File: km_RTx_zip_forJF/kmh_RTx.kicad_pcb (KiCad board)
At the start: 2 copper layers, 50 x 40 mm, 54 parts, among them IC2 UA78M33QDCYRG4Q1, J1 Conn_01x06_Pin, T1 ADT16-1T+, T2 ADT16-1T+, U1 AD4PS-1+, U2 BD00D0AWHFP-TR, X1 ASSFLP-R-C02, X2 ASSFLP-R-C02, X3 ASSFLP-R-C02, X4 ASSFLP-R-C02

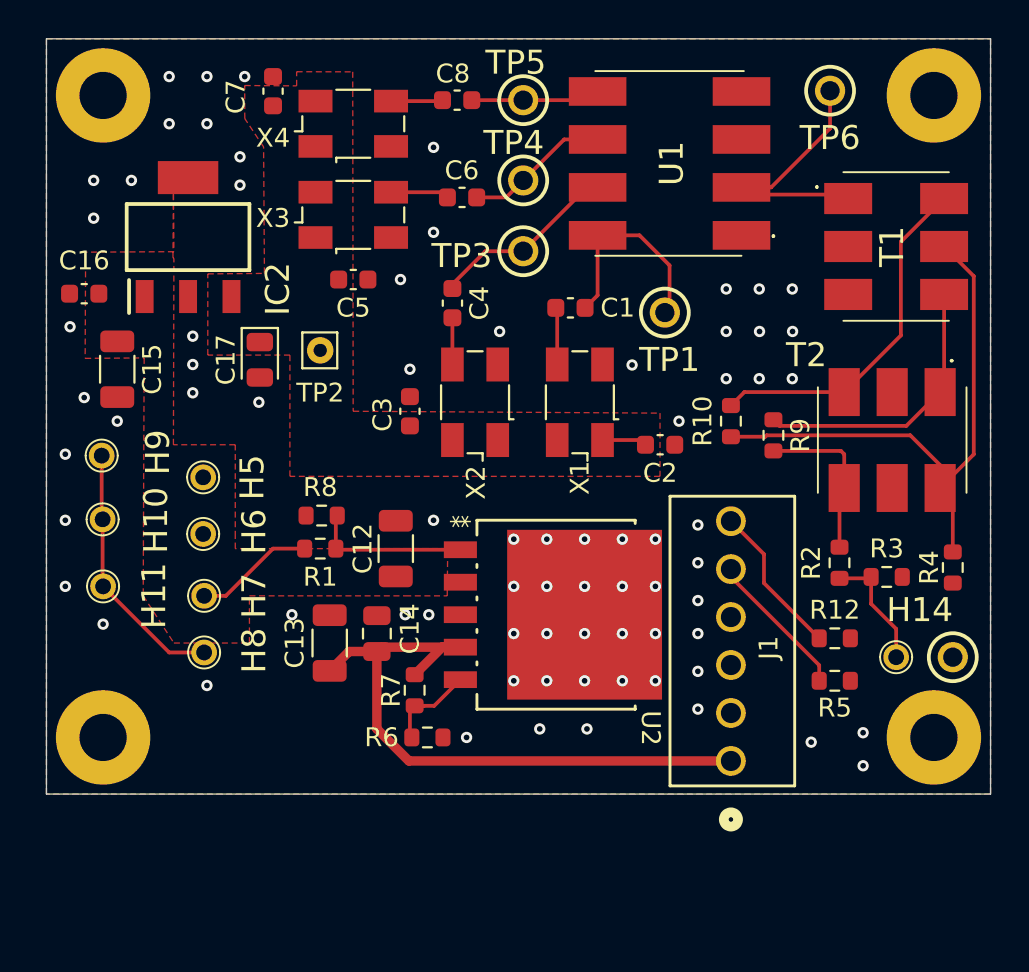
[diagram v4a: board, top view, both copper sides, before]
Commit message: added 2 bit buffers, which replace the previous 8 bit buffers
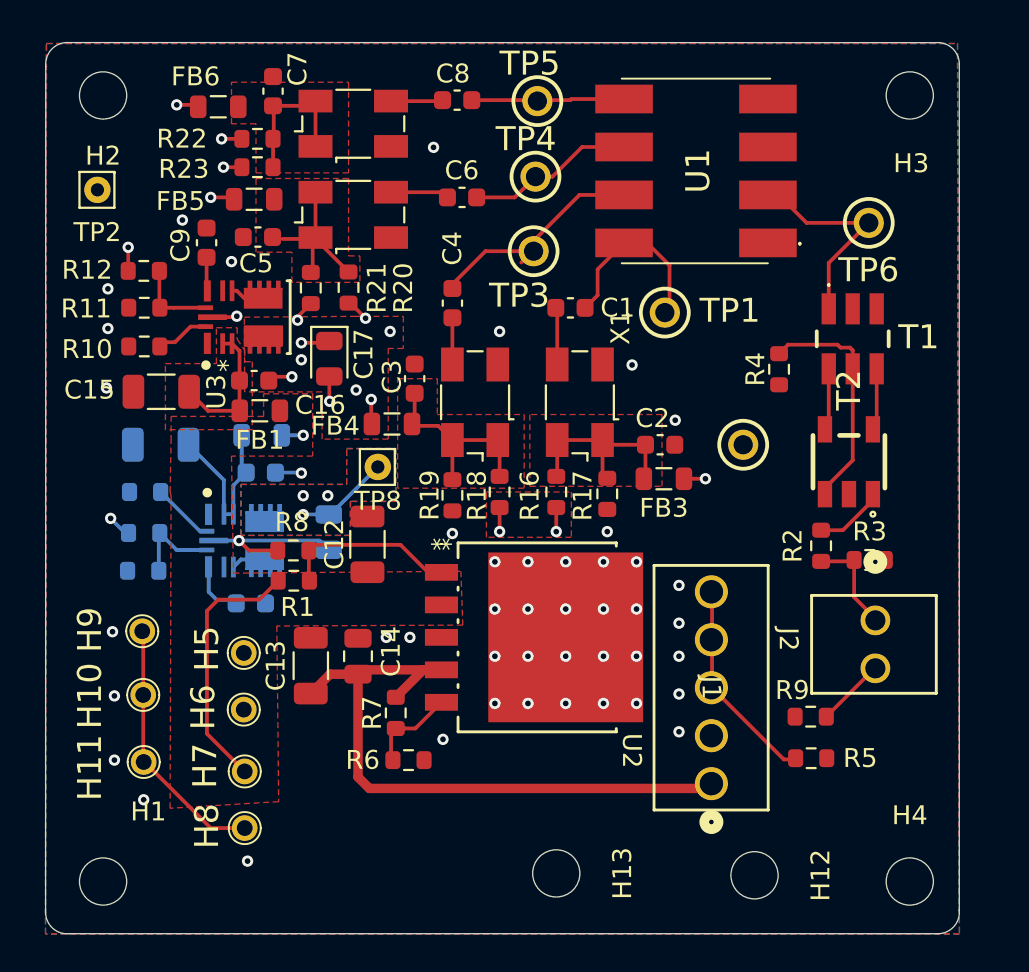
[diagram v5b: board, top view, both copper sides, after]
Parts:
- removed H14: 2111-2-00-44-00-00-07-0, Turrets:2111200440000070
- removed IC2: UA78M33QDCYRG4Q1, LDOs:SOT230P700X180-4N
- added C10: 4.7uF, Capacitor_SMD:C_1206_3216Metric, B.Cu at (94.5, 46.0)
- added C11: 0.1uF, Capacitor_SMD:C_0603_1608Metric, B.Cu at (99.8, 47.5)
- added C18: 1uF, Capacitor_SMD:C_0603_1608Metric, B.Cu at (99.3, 54.4)
- added C19: 22uF, Diode_SMD:D_0805_2012Metric, B.Cu at (103.5, 50.6)
- added C9: 1uF, Capacitor_SMD:C_0603_1608Metric, F.Cu at (97.0, 35.3)
- added FB1: FerriteBead, Inductor_SMD:L_0805_2012Metric, F.Cu at (99.8, 44.2)
- added FB2: FerriteBead, Inductor_SMD:L_0805_2012Metric, B.Cu at (99.9, 45.5)
- added FB3: FerriteBead, Inductor_SMD:L_0805_2012Metric, F.Cu at (121.2, 47.8)
- added FB4: FerriteBead, Inductor_SMD:L_0805_2012Metric, F.Cu at (106.8, 44.9)
- added FB5: FerriteBead, Inductor_SMD:L_0805_2012Metric, F.Cu at (99.5, 33.0)
- added FB6: FerriteBead, Inductor_SMD:L_0805_2012Metric, F.Cu at (97.6, 28.1)
- added H12: MountingHole, MountingHole:MountingHole_2.5mm, F.Cu at (126.0, 68.8)
- added H13: MountingHole, MountingHole:MountingHole_2.5mm, F.Cu at (115.5, 68.7)
- added J2: Conn_01x02_Pin, Connectors_kmh:22232021, F.Cu at (132.4, 55.3)
- added R11: 10k, Resistor_SMD:R_0603_1608Metric, F.Cu at (93.7, 38.7)
- added R13: 20k, Resistor_SMD:R_0603_1608Metric, B.Cu at (93.7, 48.5)
- added R14: 40.2k, Resistor_SMD:R_0603_1608Metric, B.Cu at (93.7, 50.7)
- added R15: 10k, Resistor_SMD:R_0603_1608Metric, B.Cu at (93.6, 52.7)
- added R16: R_US, Resistor_SMD:R_0603_1608Metric, F.Cu at (115.5, 48.5)
- added R17: R_US, Resistor_SMD:R_0603_1608Metric, F.Cu at (118.2, 48.6)
- added R18: R_US, Resistor_SMD:R_0603_1608Metric, F.Cu at (112.5, 48.5)
- added R19: R_US, Resistor_SMD:R_0603_1608Metric, F.Cu at (110.0, 48.7)
- added R20: R_US, Resistor_SMD:R_0603_1608Metric, F.Cu at (104.5, 37.7)
- added R21: R_US, Resistor_SMD:R_0603_1608Metric, F.Cu at (102.5, 37.7)
- added R22: R_US, Resistor_SMD:R_0603_1608Metric, F.Cu at (99.7, 29.8)
- added R23: R_US, Resistor_SMD:R_0603_1608Metric, F.Cu at (99.7, 31.3)
- added TP8: 5V, Connector_Pin:Pin_D0.7mm_L6.5mm_W1.8mm_FlatFork, F.Cu at (106.0, 47.2)
- added U3: TLVM23615RDNR, DCDC:TLVM23615, F.Cu at (99.0, 39.2)
- added U4: TLVM23615RDNR, DCDC:TLVM23615, B.Cu at (99.0, 51.1)
- C17: value 2.2uF -> 22uF
- H1, H2, H3, H4: footprint MountingHole:MountingHole_2.5mm_Pad -> MountingHole:MountingHole_2.5mm
- J1: footprint Connectors_kmh:22232061 -> Connectors_kmh:22272051
- R10: value 0 -> 20k
- R12: value 10M -> 23.2k
- R9: value 0 -> 10M
- T1: value ADT16-1T+ -> TCM8-1+; footprint RF_Componets:ADT161T -> RF_Componets:TCM81
- T2: value ADT16-1T+ -> ETC4-1-2TR; footprint RF_Componets:ADT161T -> RF_Componets:ETC4_1_2TR
- moved R12 41.4 mm to (93.7, 36.8)
- moved R10 31.3 mm to (93.7, 40.8), turned to 0 degrees
- moved TP7 15.8 mm to (125.4, 46.0)
- moved R9 15.0 mm to (129.0, 60.4), turned to 0 degrees
- moved TP2 14.5 mm to (91.2, 32.5)
- moved R4 14.0 mm to (127.3, 42.0)
- moved C16 10.1 mm to (99.5, 42.6), turned to 0 degrees
- moved H10 9.55 mm to (93.6, 59.2)
- moved H11 9.55 mm to (93.7, 62.8)
- moved H5 9.55 mm to (99.0, 57.0)
- moved H6 9.55 mm to (99.0, 60.0)
- moved H7 9.55 mm to (99.0, 63.3)
- moved H8 9.55 mm to (99.0, 66.3)
- moved H9 9.55 mm to (93.6, 55.9)
- moved H4 7.74 mm to (134.2, 69.1)
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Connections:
- C15 pad 1: +15V -> /15V_FB
- C16 pad 1: +15V -> /15V_FB
- C2 pad 1: +3.3V -> Net-(X1-Tri-State)
- C3 pad 1: +3.3V -> Net-(X2-Tri-State)
- C5 pad 1: +3.3V -> Net-(X3-Tri-State)
- C7 pad 1: +3.3V -> Net-(X4-Tri-State)
- J1 pad 3: GND -> Net-(J1-Pin_3)
- J1 pad 4: GND -> Net-(J1-Pin_3)
- J1 pad 5: Net-(J1-Pin_5) -> Net-(J1-Pin_3)
- R10 pad 1: Net-(T1-SA) -> GND
- R10 pad 2: GNDPWR -> Net-(U3-RT)
- R12 pad 1: GND -> Net-(U3-FB)
- R12 pad 2: Net-(J1-Pin_6) -> +3.3V
- R5 pad 2: Net-(J1-Pin_5) -> Net-(J1-Pin_3)
- R9 pad 1: Net-(T1-SB) -> GND
- R9 pad 2: Net-(T2-SB) -> Net-(J2-Pin_2)
- T2 pad 1: Net-(T1-SB) -> Net-(T2-SB)
- T2 pad 2: (no net) -> unconnected-(T2-SC-Pad2)
- T2 pad 3: Net-(T1-SA) -> GNDPWR
- T2 pad 4: Net-(T2-SB) -> Net-(T1-SA)
- T2 pad 5: unconnected-(T2-SC-Pad5) -> Net-(T1-SB)
- X1 pad 1: +3.3V -> Net-(X1-Tri-State)
- X1 pad 4: +3.3V -> Net-(X1-Tri-State)
- X2 pad 1: +3.3V -> Net-(X2-Tri-State)
- X2 pad 4: +3.3V -> Net-(X2-Tri-State)
- X3 pad 1: +3.3V -> Net-(X3-Tri-State)
- X3 pad 4: +3.3V -> Net-(X3-Tri-State)
- X4 pad 1: +3.3V -> Net-(X4-Tri-State)
- X4 pad 4: +3.3V -> Net-(X4-Tri-State)
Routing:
- net GNDPWR: track 30.8 -> 12.9 mm
- net GND: track 13.8 -> 30.1 mm, vias 74 -> 51
- net Net-(T1-SA): track 18.8 -> 3.29 mm
- net Net-(T1-SB): track 15.0 -> 3.29 mm
- net +5V: track 0.00 -> 11.2 mm, vias 0 -> 8
- net Net-(J1-Pin_3): track 0.00 -> 11.0 mm
- net Net-(X2-Tri-State): track 0.00 -> 10.5 mm
- net Net-(X1-Tri-State): track 0.00 -> 10.4 mm
- net /15V FB1: track 0.00 -> 9.98 mm
- net Net-(X3-Tri-State): track 0.00 -> 8.56 mm
- net Net-(X4-Tri-State): track 0.00 -> 8.54 mm
- net Net-(J1-Pin_6): track 8.14 -> 0.00 mm
- net Net-(J1-Pin_5): track 7.85 -> 0.00 mm
- net ReleaseAntenna: track 6.36 -> 13.8 mm
- net /15V_FB: track 0.00 -> 7.32 mm
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- added copper zone on In1.Cu, net +3.3V
- added copper zone on B.Cu, net +5V
- added copper zone on F.Cu, net +5V
- added copper zone on In2.Cu, net +5V
- added copper zone on F.Cu, net /15V_FB
- added copper zone on F.Cu, net Net-(X1-Tri-State)
- added copper zone on F.Cu, net Net-(X2-Tri-State)
- added copper zone on F.Cu, net Net-(X3-Tri-State)
- added copper zone on F.Cu, net Net-(X4-Tri-State)
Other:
- board size 50 x 40 mm -> 48.4 x 47.2 mm
- copper layers 2 -> 4
